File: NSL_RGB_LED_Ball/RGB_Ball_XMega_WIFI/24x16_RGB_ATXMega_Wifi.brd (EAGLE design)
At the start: 46.4 x 123.7 mm, 107 parts, among them IC2 TLC5947XLP, IC3 TLC5947XLP, IC4 TLC5947XLP, IC5 MCP73123, IC6 CC3000, IC7 MMA7455L, IC8 OPA344, X1 NX3225GA-16.000M-STD-CRG-2

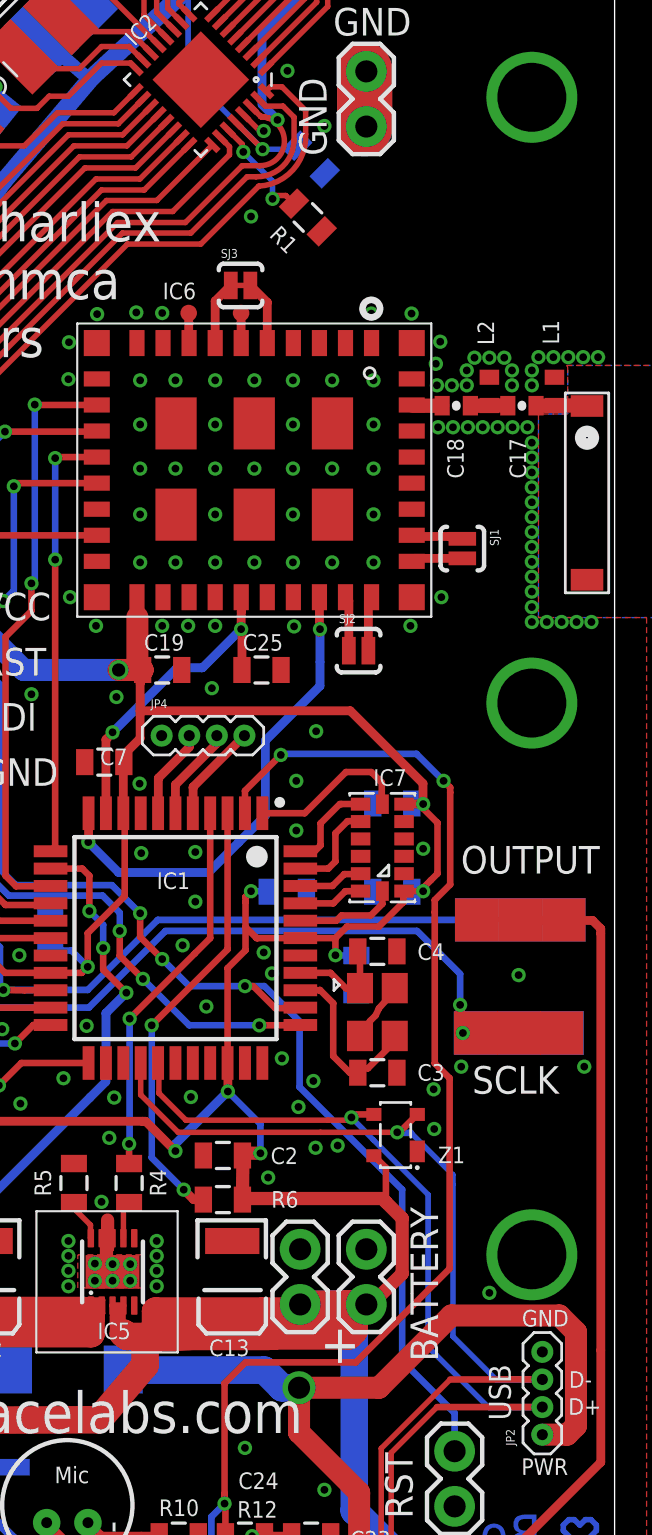
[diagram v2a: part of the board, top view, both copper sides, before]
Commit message: 
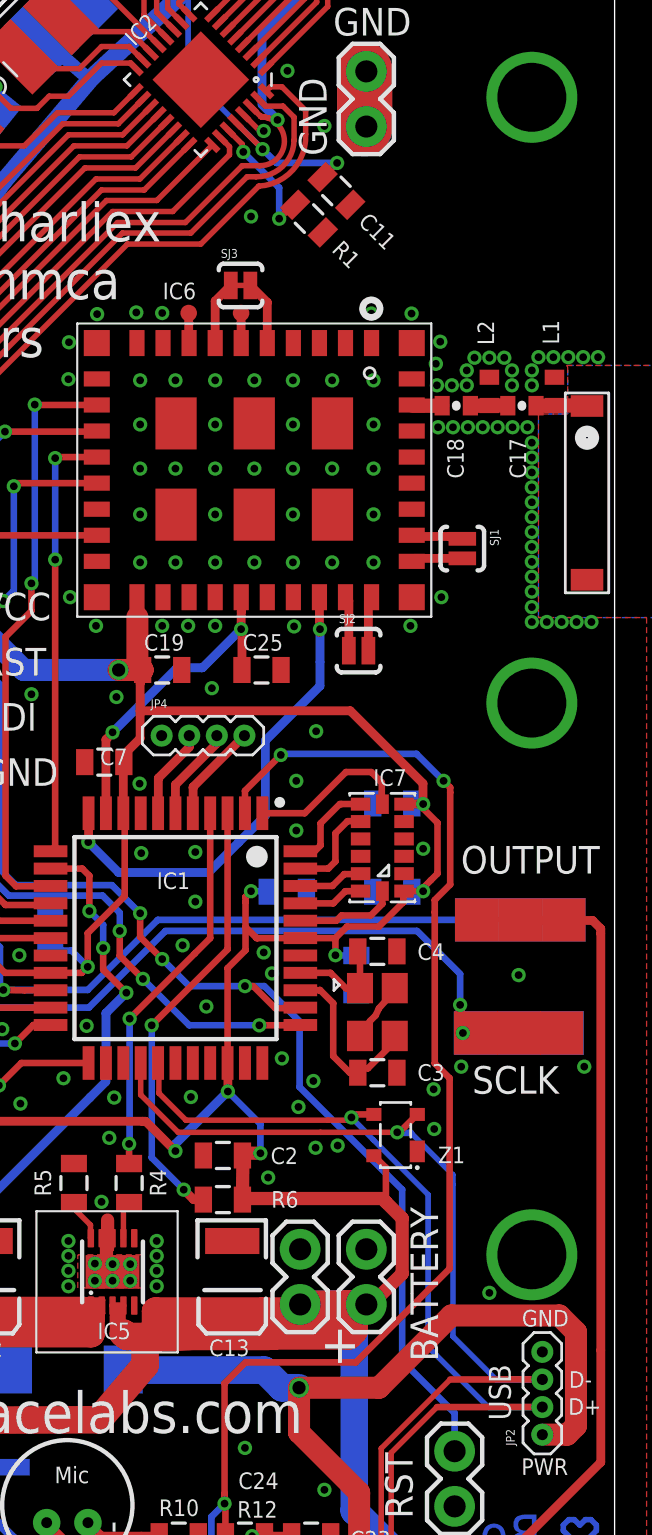
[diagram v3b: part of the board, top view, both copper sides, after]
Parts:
- moved C11 1.86 mm to (-30.6, 36.3), flipped to the top, turned to 315 degrees
- moved R1 0.07 mm to (-31.8, 35.0)
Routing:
- net VCC: track 553.3 -> 556.3 mm, vias 19 -> 20
- net HOLE: track 5.42 -> 6.25 mm
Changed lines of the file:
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@@
 <attribute name="MPN" value="" x="-36.83" y="41.402" size="1.778" layer="27" rot="R135" display="off"/>
 </element>
-<element name="R1" library="24x16_RGB" package="0805" value="20K" x="-31.8993" y="35.0568" smashed="yes" rot="R135">
-<attribute name="NAME" x="-32.2975" y="33.8621" size="0.762" layer="21" font="vector" ratio="12" rot="R135"/>
-<attribute name="VALUE" x="-29.6542" y="36.4038" size="1.27" layer="27" rot="R135"/>
-<attribute name="OC_NEWARK" value="unknown" x="-31.8993" y="35.0568" size="1.778" layer="27" rot="R135" display="off"/>
-<attribute name="MF" value="" x="-31.8993" y="35.0568" size="1.778" layer="27" rot="R135" display="off"/>
-<attribute name="MPN" value="" x="-31.8993" y="35.0568" size="1.778" layer="27" rot="R135" display="off"/>
+<element name="R1" library="24x16_RGB" package="0805" value="20K" x="-31.8485" y="35.006" smashed="yes" rot="R135">
+<attribute name="NAME" x="-30.8469" y="33.5241" size="0.762" layer="21" font="vector" ratio="12" rot="R315"/>
+<attribute name="VALUE" x="-29.6034" y="36.353" size="1.27" layer="27" rot="R135"/>
+<attribute name="OC_NEWARK" value="unknown" x="-31.8485" y="35.006" size="1.778" layer="27" rot="R135" display="off"/>
+<attribute name="MF" value="" x="-31.8485" y="35.006" size="1.778" layer="27" rot="R135" display="off"/>
+<attribute name="MPN" value="" x="-31.8485" y="35.006" size="1.778" layer="27" rot="R135" display="off"/>
 </element>
 <element name="SLOT1" library="slice" package="SLOT" value="SLOT" x="-17.78" y="-50.8" smashed="yes" rot="R180">
@@
 <attribute name="MPN" value="08055C105MAT2A" x="-43.7642" y="2.2098" size="1.778" layer="28" rot="MR90" display="off"/>
 </element>
-<element name="C11" library="slice_noshift" package="0805" value=".1uF" x="-31.756690625" y="37.725690625" smashed="yes" rot="MR225">
-<attribute name="VALUE" x="-31.487284375" y="39.4319375" size="0.4064" layer="28" rot="MR225"/>
-<attribute name="NAME" x="-31.228225" y="39.7381875" size="0.762" layer="22" font="vector" ratio="12" rot="MR225"/>
-<attribute name="VALUE" x="-31.487284375" y="39.4319375" size="0.4064" layer="28" rot="MR225"/>
-<attribute name="OC_NEWARK" value="73T5385" x="-31.756690625" y="37.725690625" size="1.778" layer="28" rot="MR225" display="off"/>
-<attribute name="MF" value="" x="-31.756690625" y="37.725690625" size="1.778" layer="28" rot="MR225" display="off"/>
-<attribute name="MPN" value="08055C105MAT2A" x="-31.756690625" y="37.725690625" size="1.778" layer="28" rot="MR225" display="off"/>
+<element name="C11" library="slice_noshift" package="0805" value=".1uF" x="-30.588290625" y="36.277890625" smashed="yes" rot="R315">
+<attribute name="VALUE" x="-32.2945375" y="36.008484375" size="0.4064" layer="27" rot="R315"/>
+<attribute name="NAME" x="-29.6289875" y="34.809625" size="0.762" layer="21" font="vector" ratio="12" rot="R315"/>
+<attribute name="VALUE" x="-32.2945375" y="36.008484375" size="0.4064" layer="27" rot="R315"/>
+<attribute name="OC_NEWARK" value="73T5385" x="-30.588290625" y="36.277890625" size="1.778" layer="27" rot="R315" display="off"/>
+<attribute name="MF" value="" x="-30.588290625" y="36.277890625" size="1.778" layer="27" rot="R315" display="off"/>
+<attribute name="MPN" value="08055C105MAT2A" x="-30.588290625" y="36.277890625" size="1.778" layer="27" rot="R315" display="off"/>
 </element>
 <element name="C15" library="24x16_RGB" package="0805" value="10uF" x="-49.784" y="-7.366" rot="MR270">
@@
 <wire x1="-27.2288" y1="-27.0256" x2="-24.6888" y2="-29.5656" width="1.27" layer="16"/>
 <wire x1="-24.6888" y1="-29.5656" x2="-24.6888" y2="-40.1066" width="1.27" layer="16"/>
-<wire x1="-32.3930875" y1="38.362084375" x2="-32.553571875" y2="38.2016" width="0.254" layer="16"/>
-<wire x1="-32.553571875" y1="38.2016" x2="-33.9852" y2="38.2016" width="0.254" layer="16"/>
 <wire x1="-26.6004" y1="8.0452" x2="-26.6004" y2="8.9982" width="0.4064" layer="1"/>
 <wire x1="-27.4668" y1="8.0518" x2="-26.5938" y2="8.0518" width="0.4064" layer="1"/>
@@
 <wire x1="-49.276" y1="2.4384" x2="-49.5444" y2="2.7068" width="0.3048" layer="1"/>
 <wire x1="-49.5444" y1="2.7068" x2="-50.673" y2="2.7068" width="0.3048" layer="1"/>
+<via x="-30.5562" y="37.5666" extent="1-16" drill="0.3556"/>
+<wire x1="-30.5562" y1="37.5666" x2="-31.224684375" y2="36.923515625" width="0.3048" layer="1"/>
+<wire x1="-31.224684375" y1="36.923515625" x2="-31.224684375" y2="36.914284375" width="0.3048" layer="1"/>
+<wire x1="-33.9852" y1="38.2016" x2="-33.3502" y2="37.5666" width="0.3048" layer="16"/>
+<wire x1="-33.3502" y1="37.5666" x2="-30.5562" y2="37.5666" width="0.3048" layer="16"/>
 </signal>
 <signal name="COL2">
@@
 <via x="-34.8742" y="38.0746" extent="1-16" drill="0.3556"/>
 <wire x1="-34.8742" y1="37.939696875" x2="-34.8742" y2="38.0746" width="0.254" layer="16"/>
-<wire x1="-32.53569375" y1="35.69319375" x2="-32.9184" y2="36.068" width="0.254" layer="1"/>
-<wire x1="-32.9184" y1="36.068" x2="-33.4772" y2="36.068" width="0.254" layer="1"/>
-<wire x1="-33.4772" y1="36.068" x2="-33.528" y2="35.9156" width="0.254" layer="1"/>
-<via x="-33.528" y="35.9156" extent="1-16" drill="0.3556"/>
-<wire x1="-33.528" y1="35.9156" x2="-33.528" y2="36.7284" width="0.254" layer="16"/>
-<wire x1="-33.528" y1="36.7284" x2="-34.8742" y2="38.0746" width="0.254" layer="16"/>
+<via x="-33.2232" y="35.0012" extent="1-16" drill="0.3556"/>
+<wire x1="-33.2232" y1="35.0012" x2="-32.55660625" y2="35.69319375" width="0.3048" layer="1"/>
+<wire x1="-32.55660625" y1="35.69319375" x2="-32.48489375" y2="35.64239375" width="0.3048" layer="1"/>
+<wire x1="-34.8742" y1="38.0746" x2="-33.2232" y2="36.4236" width="0.3048" layer="16"/>
+<wire x1="-33.2232" y1="36.4236" x2="-33.2232" y2="35.0012" width="0.3048" layer="16"/>
 </signal>
 <signal name="COL22">
@@
 <contactref element="D1" pad="A"/>
 <wire x1="-29.5402" y1="-32.2072" x2="-29.5402" y2="-23.6474" width="1.016" layer="1"/>
-<via x="-32.3088" y="-18.8214" extent="1-16" drill="1.016"/>
+<via x="-32.3088" y="-18.8214" extent="1-16" drill="0.6096"/>
 <wire x1="-28.5242" y1="-34.3916" x2="-27.3812" y2="-34.3916" width="1.016" layer="1"/>
 <wire x1="-25.6902" y1="-34.3914" x2="-27.229" y2="-34.3914" width="0.3048" layer="1"/>

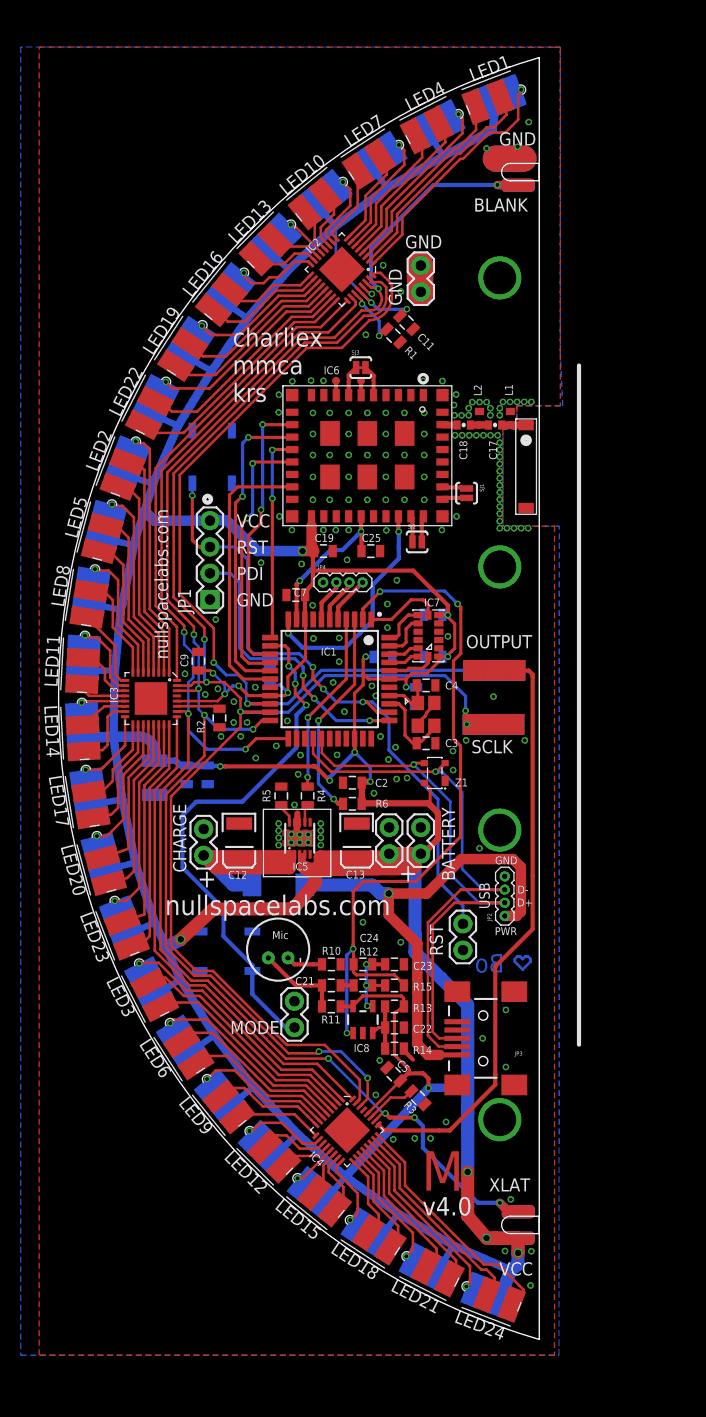
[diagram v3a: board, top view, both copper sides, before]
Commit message: 
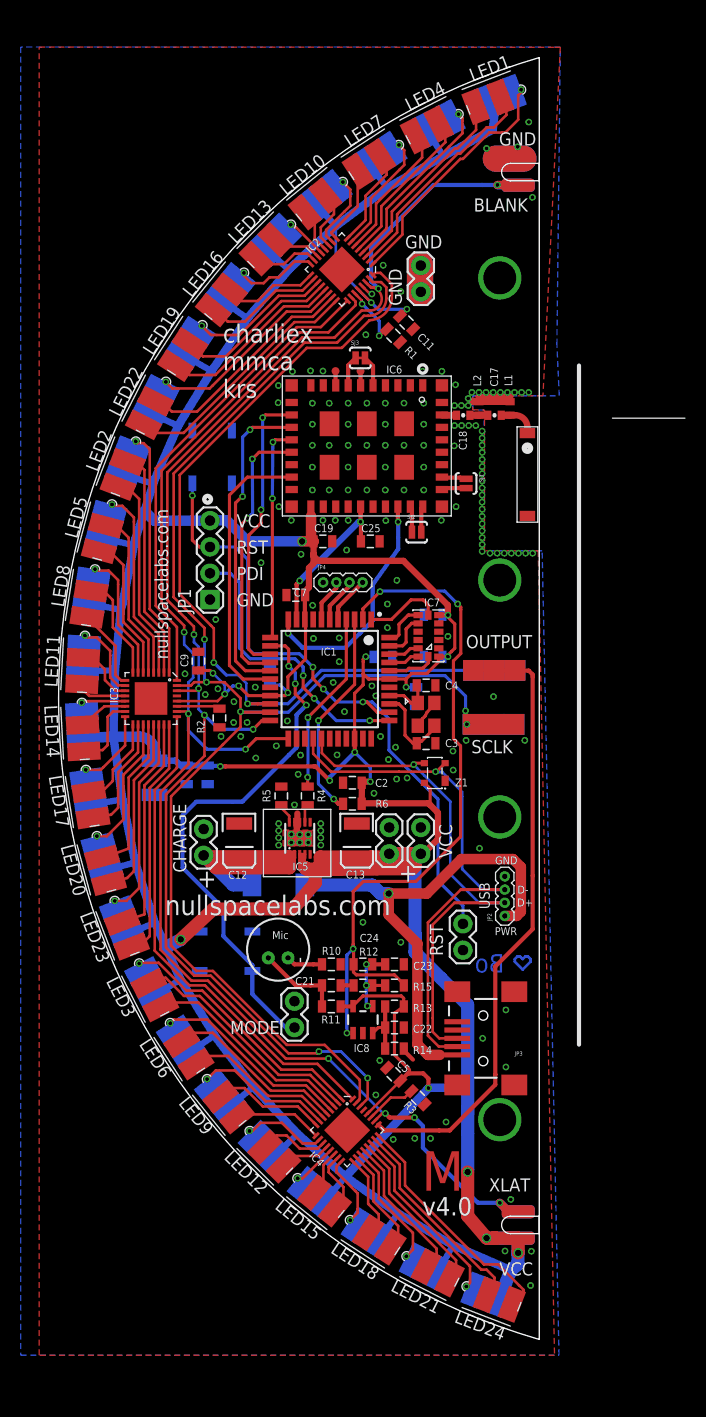
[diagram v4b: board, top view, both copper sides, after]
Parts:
- moved SJ3 0.94 mm to (-35.1, 32.9)
- moved C17 0.94 mm to (-22.1, 27.3)
- moved C18 0.94 mm to (-25.1, 27.3)
- moved L1 0.94 mm to (-20.6, 28.0)
- moved L2 0.94 mm to (-23.6, 28.0)
- moved SJ2 0.94 mm to (-29.6, 16.1)
- moved C19 0.94 mm to (-38.7, 15.2)
- moved C25 0.94 mm to (-34.1, 15.2)
- moved IC6 0.94 mm to (-42.6, 31.1)
- moved TP13 0.94 mm to (-35.0, 31.6)
- moved SJ1 0.94 mm to (-24.8, 20.8)
- moved TP14 0.94 mm to (-37.4, 31.6)
- moved ANT 0.77 mm to (-18.9, 21.6)
- renumbered BATTERY to VCC
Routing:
- net GND: track 16.7 -> 29.4 mm, vias 167 -> 170
- net VCC: track 556.3 -> 557.5 mm
- net N$25: track 2.48 -> 3.61 mm
- net SPI_IRQ: track 20.1 -> 20.9 mm
- net MISO: track 30.1 -> 30.8 mm
- net SS: track 27.4 -> 28.2 mm
- net VBAT_SW_EN: track 22.6 -> 23.2 mm
- net MOSI: track 26.0 -> 26.6 mm

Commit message: 
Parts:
- R1, R2, R3: value 20K -> 24K
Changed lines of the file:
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@@
 <attribute name="MPN" value="" x="-36.83" y="41.402" size="1.778" layer="27" rot="R135" display="off"/>
 </element>
-<element name="R1" library="24x16_RGB" package="0805" value="20K" x="-31.8485" y="35.006" smashed="yes" rot="R135">
+<element name="R1" library="24x16_RGB" package="0805" value="24K" x="-31.8485" y="35.006" smashed="yes" rot="R135">
 <attribute name="NAME" x="-30.8469" y="33.5241" size="0.762" layer="21" font="vector" ratio="12" rot="R315"/>
 <attribute name="VALUE" x="-29.6034" y="36.353" size="1.27" layer="27" rot="R135"/>
@@
 <attribute name="MPN" value="" x="-55.245" y="0" size="1.778" layer="27" rot="R180" display="off"/>
 </element>
-<element name="R2" library="24x16_RGB" package="0805" value="20K" x="-48.641" y="-1.8796" smashed="yes" rot="R90">
+<element name="R2" library="24x16_RGB" package="0805" value="24K" x="-48.641" y="-1.8796" smashed="yes" rot="R90">
 <attribute name="NAME" x="-50.0634" y="-3.3528" size="0.762" layer="21" font="vector" ratio="12" rot="R90"/>
 <attribute name="VALUE" x="-46.101" y="-2.5146" size="1.27" layer="27" rot="R90"/>
@@
 <attribute name="MPN" value="" x="-36.322" y="-41.656" size="1.778" layer="27" rot="R225" display="off"/>
 </element>
-<element name="R3" library="24x16_RGB" package="0805" value="20K" x="-29.4734" y="-38.5303" smashed="yes" rot="R135">
+<element name="R3" library="24x16_RGB" package="0805" value="24K" x="-29.4734" y="-38.5303" smashed="yes" rot="R135">
 <attribute name="NAME" x="-29.516" y="-39.6488" size="0.762" layer="21" font="vector" ratio="12" rot="R135"/>
 <attribute name="VALUE" x="-27.2283" y="-37.1833" size="1.27" layer="27" rot="R135"/>

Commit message: 
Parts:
- R1, R2, R3: value 24K -> 47K
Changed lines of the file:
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@@
 <attribute name="MPN" value="" x="-36.83" y="41.402" size="1.778" layer="27" rot="R135" display="off"/>
 </element>
-<element name="R1" library="24x16_RGB" package="0805" value="24K" x="-31.8485" y="35.006" smashed="yes" rot="R135">
+<element name="R1" library="24x16_RGB" package="0805" value="47K" x="-31.8485" y="35.006" smashed="yes" rot="R135">
 <attribute name="NAME" x="-30.8469" y="33.5241" size="0.762" layer="21" font="vector" ratio="12" rot="R315"/>
 <attribute name="VALUE" x="-29.6034" y="36.353" size="1.27" layer="27" rot="R135"/>
@@
 <attribute name="MPN" value="" x="-55.245" y="0" size="1.778" layer="27" rot="R180" display="off"/>
 </element>
-<element name="R2" library="24x16_RGB" package="0805" value="24K" x="-48.641" y="-1.8796" smashed="yes" rot="R90">
+<element name="R2" library="24x16_RGB" package="0805" value="47K" x="-48.641" y="-1.8796" smashed="yes" rot="R90">
 <attribute name="NAME" x="-50.0634" y="-3.3528" size="0.762" layer="21" font="vector" ratio="12" rot="R90"/>
 <attribute name="VALUE" x="-46.101" y="-2.5146" size="1.27" layer="27" rot="R90"/>
@@
 <attribute name="MPN" value="" x="-36.322" y="-41.656" size="1.778" layer="27" rot="R225" display="off"/>
 </element>
-<element name="R3" library="24x16_RGB" package="0805" value="24K" x="-29.4734" y="-38.5303" smashed="yes" rot="R135">
+<element name="R3" library="24x16_RGB" package="0805" value="47K" x="-29.4734" y="-38.5303" smashed="yes" rot="R135">
 <attribute name="NAME" x="-29.516" y="-39.6488" size="0.762" layer="21" font="vector" ratio="12" rot="R135"/>
 <attribute name="VALUE" x="-27.2283" y="-37.1833" size="1.27" layer="27" rot="R135"/>
